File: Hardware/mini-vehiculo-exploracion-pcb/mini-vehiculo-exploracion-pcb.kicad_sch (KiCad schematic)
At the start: 19 parts, among them IC1 BME690, J1 ArducamMINIOV2640, U1 BNO086, U2 ESP32-S3-WROOM-1, Y1 830003000

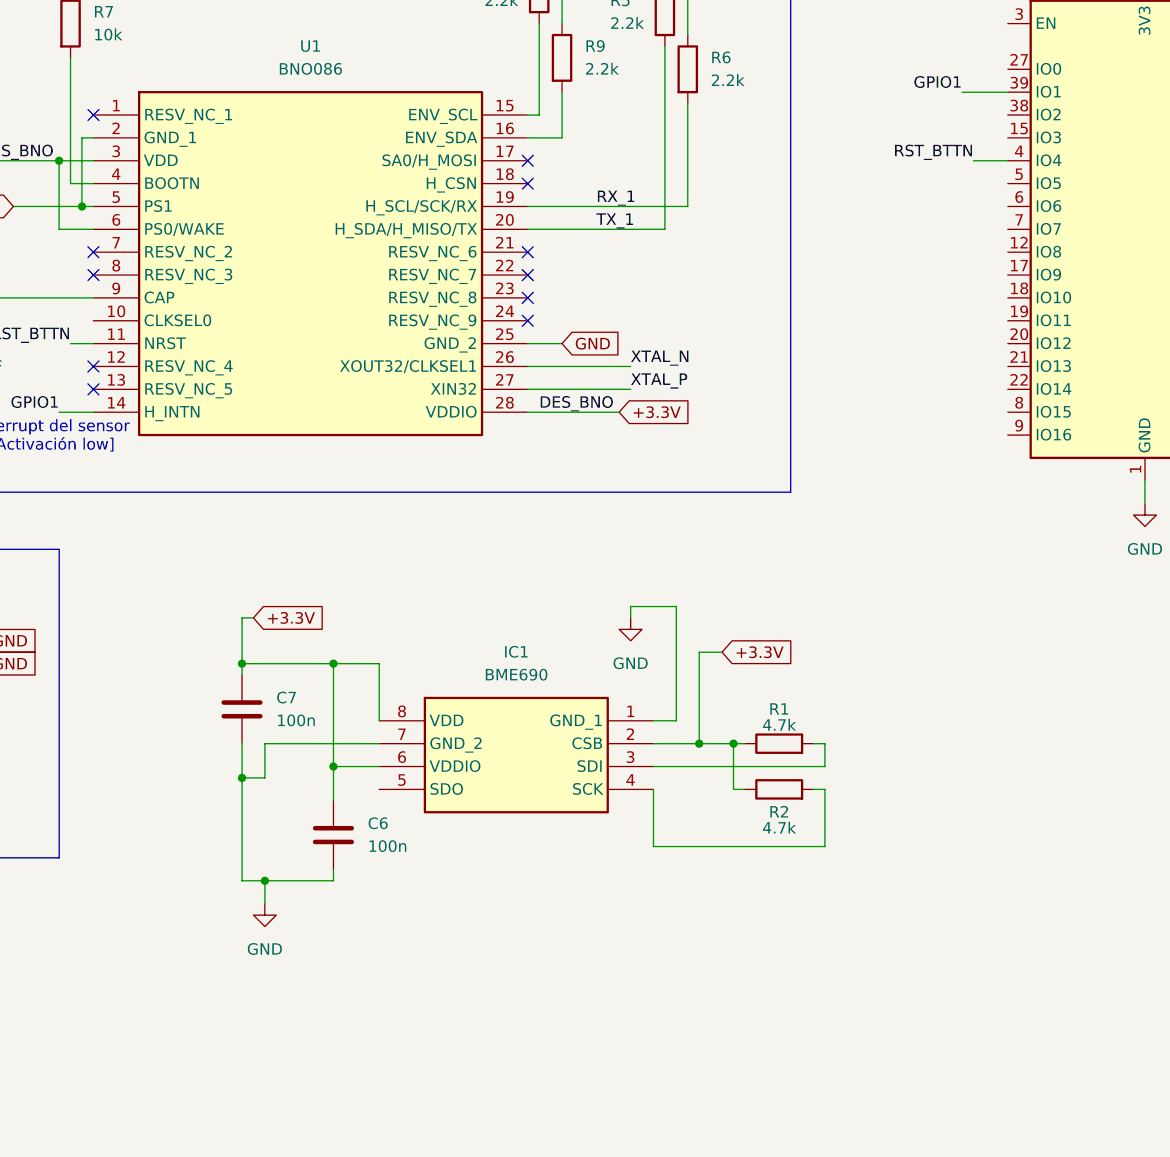
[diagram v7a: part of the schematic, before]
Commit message: Update mini-vehiculo-exploracion-pcb.kicad_sch
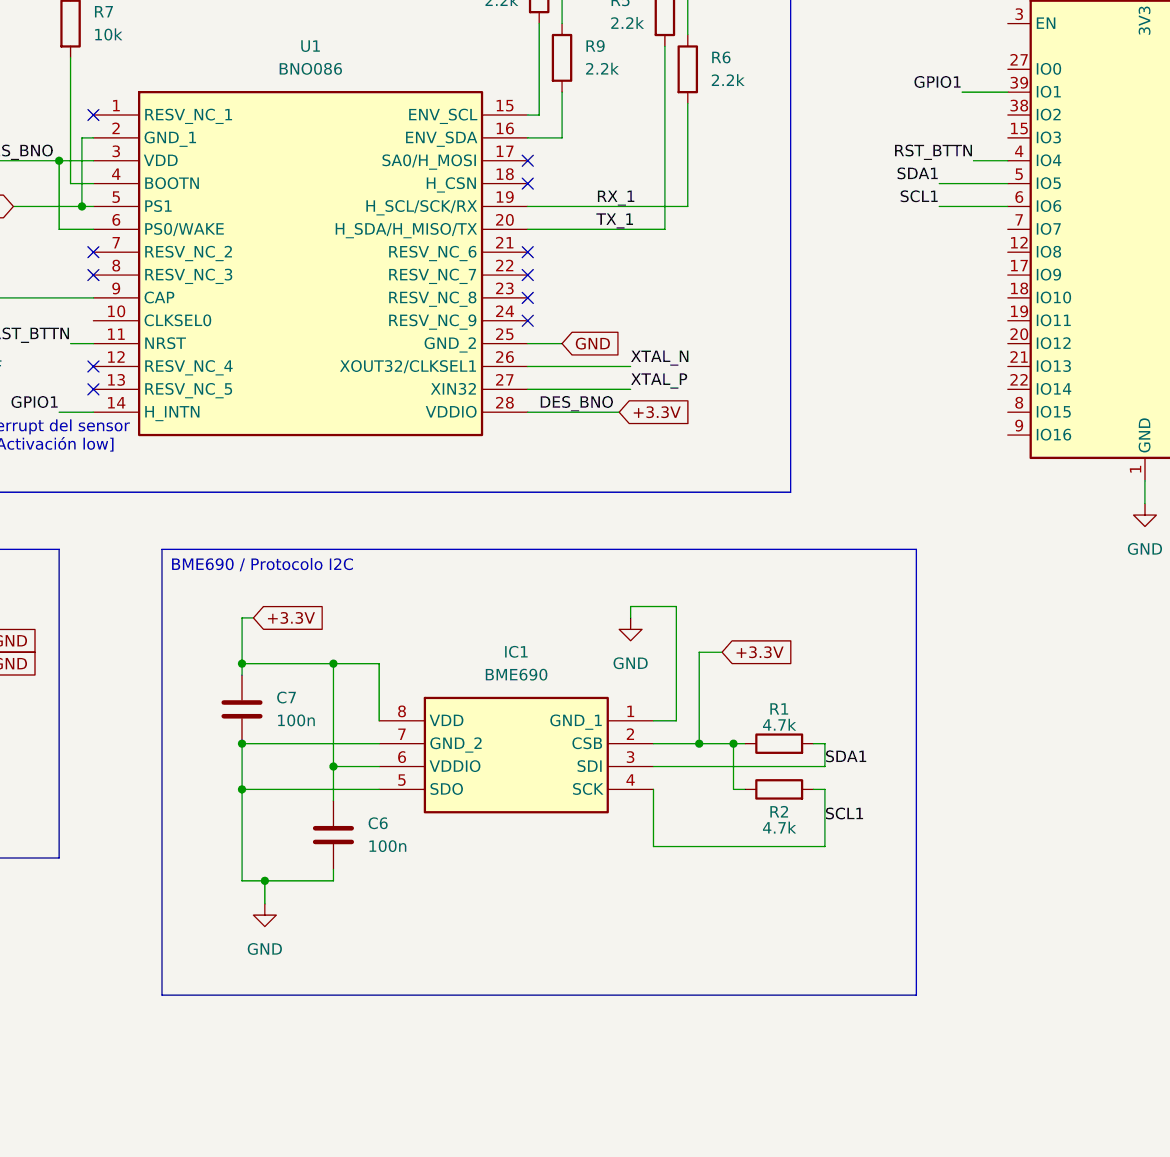
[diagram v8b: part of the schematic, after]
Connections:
- net GND: now also IC1.5 (SDO)
- net SDA1: now reaches IC1.3 (SDI), R1.2
- net SDA1: now also U2.5 (IO5)
- net SCL1: now reaches IC1.4 (SCK), R2.2
- net SCL1: now also U2.6 (IO6)
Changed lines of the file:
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@@
+		)
+	)
+	(text_box "BME690 / Protocolo I2C"
+		(exclude_from_sim no)
+		(at 91.44 90.17 0)
+		(size 83.82 49.53)
+		(margins 0.9525 0.9525 0.9525 0.9525)
+		(stroke
+			(width 0)
+			(type solid)
+		)
+		(fill
+			(type none)
+		)
+		(effects
+			(font
+				(size 1.27 1.27)
+			)
+			(justify left top)
 		)
 	)
@@
 	)
 	(junction
+		(at 100.33 111.76)
+		(diameter 0)
+		(color 0 0 0 0)
+	)
+	(junction
 		(at 110.49 102.87)
 		(diameter 0)
@@
 	)
 	(junction
-		(at 100.33 115.57)
-		(diameter 0)
-		(color 0 0 0 0)
-	)
-	(junction
 		(at 149.86 24.13)
 		(diameter 0)
@@
 	)
 	(junction
+		(at 100.33 116.84)
+		(diameter 0)
+		(color 0 0 0 0)
+	)
+	(junction
 		(at 102.87 127)
 		(diameter 0)
@@
 	(wire
 		(pts
-			(xy 102.87 115.57) (xy 100.33 115.57)
+			(xy 100.33 111.76) (xy 115.57 111.76)
 		)
 		(stroke
@@
 	(wire
 		(pts
-			(xy 100.33 111.76) (xy 100.33 115.57)
+			(xy 100.33 111.76) (xy 100.33 116.84)
 		)
 		(stroke
@@
 	(wire
 		(pts
-			(xy 102.87 111.76) (xy 102.87 115.57)
-		)
-		(stroke
-			(width 0)
-			(type default)
-		)
-	)
-	(wire
-		(pts
 			(xy 146.05 123.19) (xy 165.1 123.19)
 		)
@@
 	(wire
 		(pts
-			(xy 100.33 115.57) (xy 100.33 127)
-		)
-		(stroke
-			(width 0)
-			(type default)
-		)
-	)
-	(wire
-		(pts
 			(xy 110.49 114.3) (xy 110.49 102.87)
 		)
@@
 	(wire
 		(pts
-			(xy 115.57 111.76) (xy 102.87 111.76)
-		)
-		(stroke
-			(width 0)
-			(type default)
-		)
-	)
-	(wire
-		(pts
 			(xy 102.87 127) (xy 102.87 129.54)
 		)
@@
 	(wire
 		(pts
+			(xy 177.8 49.53) (xy 185.42 49.53)
+		)
+		(stroke
+			(width 0)
+			(type default)
+		)
+	)
+	(wire
+		(pts
 			(xy 181.61 46.99) (xy 185.42 46.99)
 		)
@@
 	(wire
 		(pts
+			(xy 177.8 52.07) (xy 185.42 52.07)
+		)
+		(stroke
+			(width 0)
+			(type default)
+		)
+	)
+	(wire
+		(pts
 			(xy 148.59 109.22) (xy 148.59 96.52)
 		)
@@
 	(wire
 		(pts
+			(xy 100.33 116.84) (xy 100.33 127)
+		)
+		(stroke
+			(width 0)
+			(type default)
+		)
+	)
+	(wire
+		(pts
 			(xy 151.13 111.76) (xy 154.94 111.76)
 		)
@@
 	(wire
 		(pts
+			(xy 100.33 116.84) (xy 115.57 116.84)
+		)
+		(stroke
+			(width 0)
+			(type default)
+		)
+	)
+	(wire
+		(pts
 			(xy 143.51 96.52) (xy 143.51 97.79)
 		)
@@
 			(width 0)
 			(type default)
+		)
+	)
+	(label "SDA1"
+		(at 177.8 49.53 180)
+		(effects
+			(font
+				(size 1.27 1.27)
+			)
+			(justify right bottom)
 		)
 	)
@@
 		)
 	)
+	(label "SDA1"
+		(at 165.1 114.3 0)
+		(effects
+			(font
+				(size 1.27 1.27)
+			)
+			(justify left bottom)
+		)
+	)
 	(label "GPIO1"
 		(at 180.34 39.37 180)
@@
 		)
 	)
+	(label "SCL1"
+		(at 177.8 52.07 180)
+		(effects
+			(font
+				(size 1.27 1.27)
+			)
+			(justify right bottom)
+		)
+	)
 	(label "XTAL_P"
 		(at 143.51 72.39 0)
 		(effects
 			(font
+				(size 1.27 1.27)
+			)
+			(justify left bottom)
+		)
+	)
+	(label "SCL1"
+		(at 165.1 120.65 0)
+		(effects
+			(font
